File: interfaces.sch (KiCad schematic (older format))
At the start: 63 parts, among them J4 WE_629105150521, J6 685119134923, J7 1140084168, U12 FT2232HQ

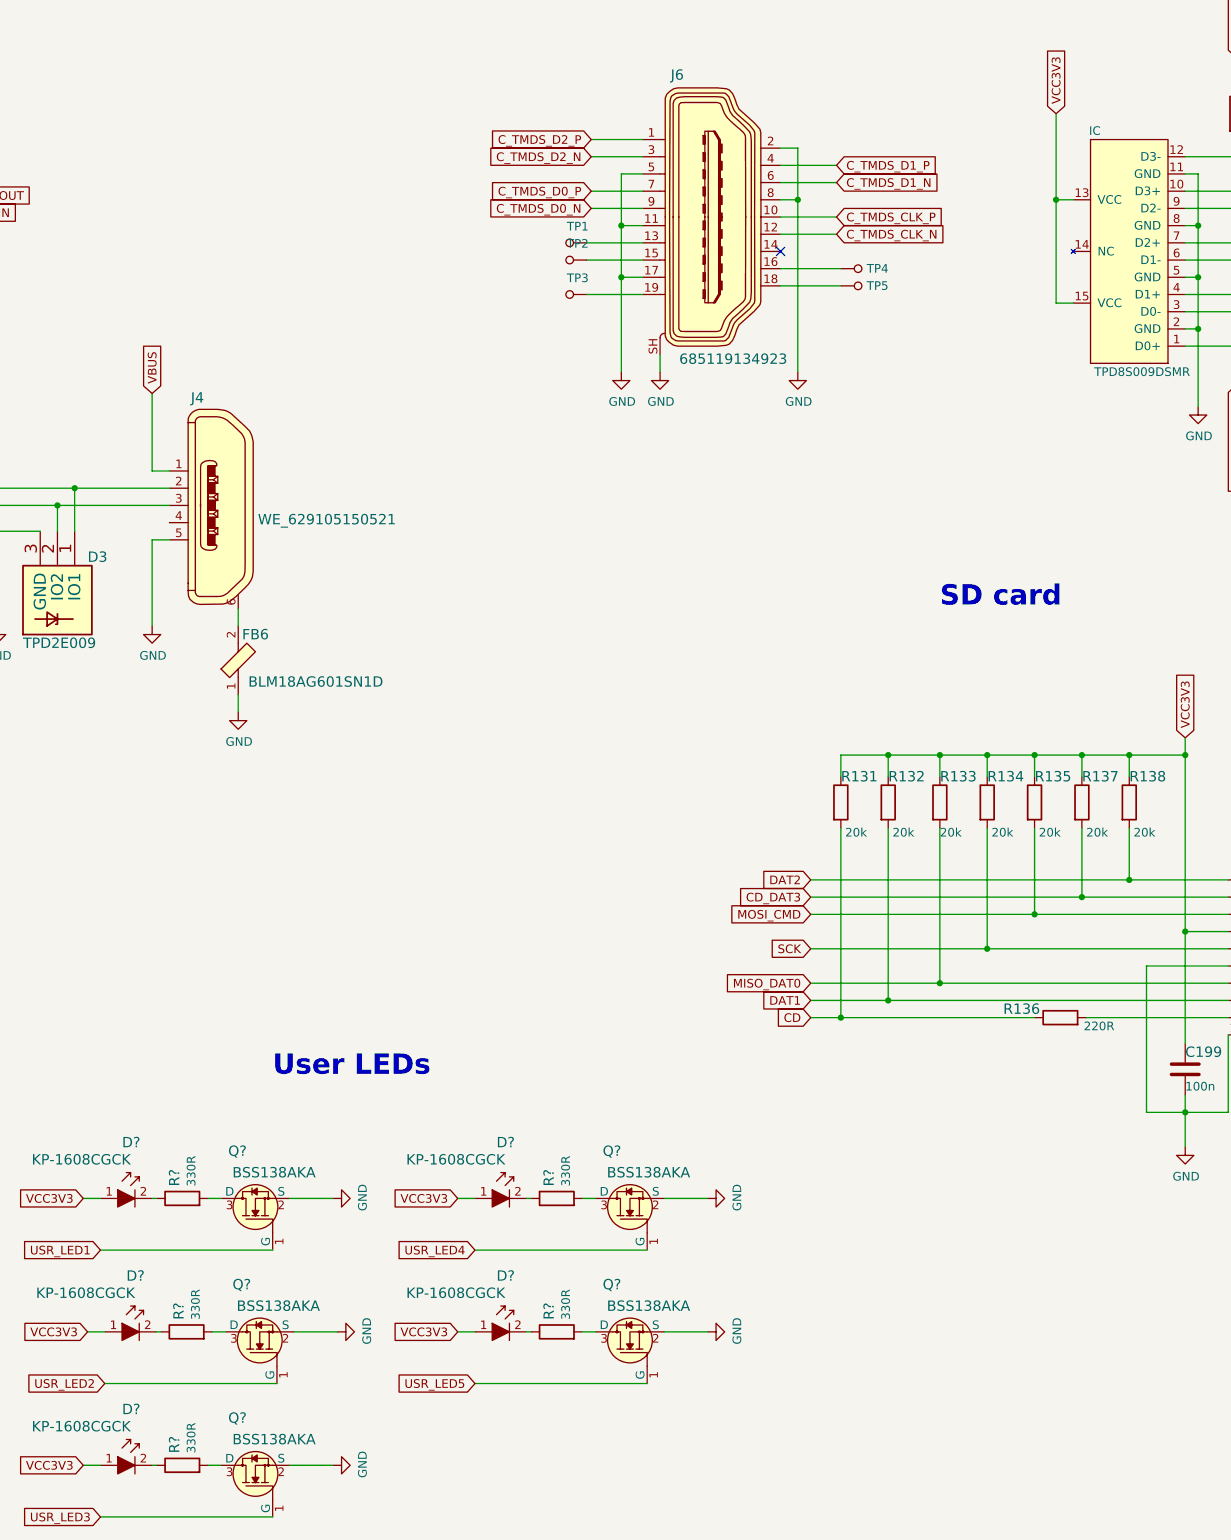
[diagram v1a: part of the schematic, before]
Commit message: Library cleanup, add RGMII layout
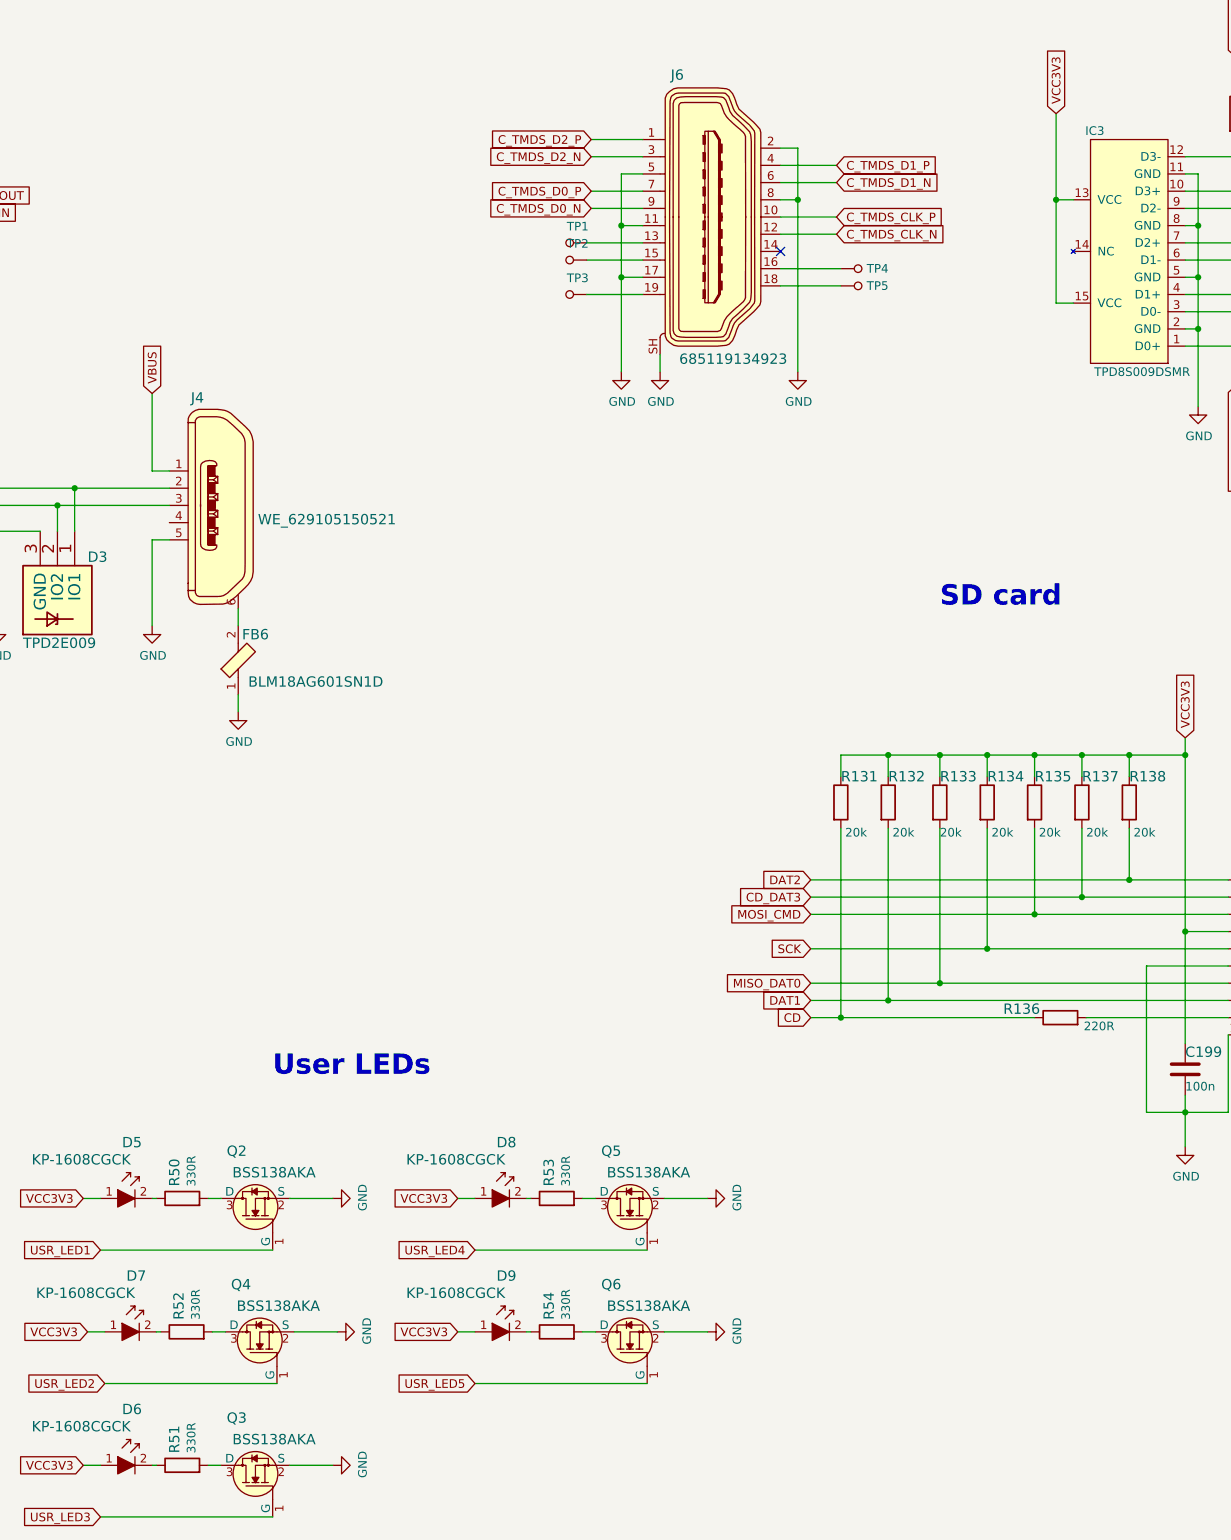
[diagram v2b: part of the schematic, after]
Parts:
- gave numbers to parts that had none: 15
- renumbered IC to IC3
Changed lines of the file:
@@
 $EndComp
 $Comp
-L lpddr4-test-board:TPD8S009DSMR IC
+L lpddr4-test-board:TPD8S009DSMR IC3
 U 1 1 601C2CA9
 P 13000 3625
-F 0 "IC" H 13225 2625 50  0000 C CNN
+F 0 "IC3" H 13225 2625 50  0000 C CNN
 F 1 "TPD8S009DSMR" H 12950 4025 50  0000 C CNN
 F 2 "lpddr4-test-board-footprints:R-PDSO-N15" H 14400 3275 50  0001 C CNN
@@
 	7800 5900 7800 6000
 $Comp
-L lpddr4-test-board:BSS138AKA Q?
+L lpddr4-test-board:BSS138AKA Q2
 U 1 1 5FF5BCFF
 P 7900 8825
-F 0 "Q?" V 8175 8875 60  0000 L CNN
+F 0 "Q2" V 8175 8875 60  0000 L CNN
 F 1 "BSS138AKA" V 8050 8475 60  0000 L CNN
 F 2 "lpddr4-test-board-footprints:SOT-23-3" H 8100 9025 60  0001 L CNN
@@
 $EndComp
 $Comp
-L lpddr4-test-board:GND #PWR?
+L lpddr4-test-board:GND #PWR0167
 U 1 1 5FF5DE33
 P 8350 8825
-F 0 "#PWR?" H 8350 8575 50  0001 C CNN
+F 0 "#PWR0167" H 8350 8575 50  0001 C CNN
 F 1 "GND" H 8355 8652 50  0000 C CNN
 F 2 "" H 8350 8825 50  0001 C CNN
@@
 	7700 8825 7625 8825
 $Comp
-L lpddr4-test-board:R_330R_0402 R?
+L lpddr4-test-board:R_330R_0402 R50
 U 1 1 5FF78200
 P 7475 8825
-F 0 "R?" V 7430 8895 60  0000 L CNN
+F 0 "R50" V 7430 8895 60  0000 L CNN
 F 1 "R_330R_0402" H 7475 8675 60  0001 C CNN
 F 2 "lpddr4-test-board-footprints:0402-res" H 7675 9025 60  0001 L CNN
@@
 $EndComp
 $Comp
-L lpddr4-test-board:KP-1608CGCK D?
+L lpddr4-test-board:KP-1608CGCK D5
 U 1 1 5FF856A4
 P 7200 8825
-F 0 "D?" H 7125 9150 60  0000 L CNN
+F 0 "D5" H 7125 9150 60  0000 L CNN
 F 1 "KP-1608CGCK" H 6600 9050 60  0000 L CNN
 F 2 "lpddr4-test-board-footprints:LED_0603" H 7400 9025 60  0001 L CNN
@@
 	8000 9125 7000 9125
 $Comp
-L lpddr4-test-board:BSS138AKA Q?
+L lpddr4-test-board:BSS138AKA Q4
 U 1 1 6002240B
 P 7925 9600
-F 0 "Q?" V 8200 9650 60  0000 L CNN
+F 0 "Q4" V 8200 9650 60  0000 L CNN
 F 1 "BSS138AKA" V 8075 9250 60  0000 L CNN
 F 2 "lpddr4-test-board-footprints:SOT-23-3" H 8125 9800 60  0001 L CNN
@@
 $EndComp
 $Comp
-L lpddr4-test-board:GND #PWR?
+L lpddr4-test-board:GND #PWR0168
 U 1 1 60022411
 P 8375 9600
-F 0 "#PWR?" H 8375 9350 50  0001 C CNN
+F 0 "#PWR0168" H 8375 9350 50  0001 C CNN
 F 1 "GND" H 8380 9427 50  0000 C CNN
 F 2 "" H 8375 9600 50  0001 C CNN
@@
 	7725 9600 7650 9600
 $Comp
-L lpddr4-test-board:R_330R_0402 R?
+L lpddr4-test-board:R_330R_0402 R52
 U 1 1 6002241C
 P 7500 9600
-F 0 "R?" V 7455 9670 60  0000 L CNN
+F 0 "R52" V 7455 9670 60  0000 L CNN
 F 1 "R_330R_0402" H 7500 9450 60  0001 C CNN
 F 2 "lpddr4-test-board-footprints:0402-res" H 7700 9800 60  0001 L CNN
@@
 $EndComp
 $Comp
-L lpddr4-test-board:KP-1608CGCK D?
+L lpddr4-test-board:KP-1608CGCK D7
 U 1 1 60022424
 P 7225 9600
-F 0 "D?" H 7150 9925 60  0000 L CNN
+F 0 "D7" H 7150 9925 60  0000 L CNN
 F 1 "KP-1608CGCK" H 6625 9825 60  0000 L CNN
 F 2 "lpddr4-test-board-footprints:LED_0603" H 7425 9800 60  0001 L CNN
@@
 	8025 9900 7025 9900
 $Comp
-L lpddr4-test-board:BSS138AKA Q?
+L lpddr4-test-board:BSS138AKA Q5
 U 1 1 600304B1
 P 10075 8825
-F 0 "Q?" V 10350 8875 60  0000 L CNN
+F 0 "Q5" V 10350 8875 60  0000 L CNN
 F 1 "BSS138AKA" V 10225 8475 60  0000 L CNN
 F 2 "lpddr4-test-board-footprints:SOT-23-3" H 10275 9025 60  0001 L CNN
@@
 $EndComp
 $Comp
-L lpddr4-test-board:GND #PWR?
+L lpddr4-test-board:GND #PWR0169
 U 1 1 600304B7
 P 10525 8825
-F 0 "#PWR?" H 10525 8575 50  0001 C CNN
+F 0 "#PWR0169" H 10525 8575 50  0001 C CNN
 F 1 "GND" H 10530 8652 50  0000 C CNN
 F 2 "" H 10525 8825 50  0001 C CNN
@@
 	9875 8825 9800 8825
 $Comp
-L lpddr4-test-board:R_330R_0402 R?
+L lpddr4-test-board:R_330R_0402 R53
 U 1 1 600304C2
 P 9650 8825
-F 0 "R?" V 9605 8895 60  0000 L CNN
+F 0 "R53" V 9605 8895 60  0000 L CNN
 F 1 "R_330R_0402" H 9650 8675 60  0001 C CNN
 F 2 "lpddr4-test-board-footprints:0402-res" H 9850 9025 60  0001 L CNN
@@
 $EndComp
 $Comp
-L lpddr4-test-board:KP-1608CGCK D?
+L lpddr4-test-board:KP-1608CGCK D8
 U 1 1 600304CA
 P 9375 8825
-F 0 "D?" H 9300 9150 60  0000 L CNN
+F 0 "D8" H 9300 9150 60  0000 L CNN
 F 1 "KP-1608CGCK" H 8775 9050 60  0000 L CNN
 F 2 "lpddr4-test-board-footprints:LED_0603" H 9575 9025 60  0001 L CNN
@@
 	10175 9125 9175 9125
 $Comp
-L lpddr4-test-board:BSS138AKA Q?
+L lpddr4-test-board:BSS138AKA Q6
 U 1 1 6003D8CD
 P 10075 9600
-F 0 "Q?" V 10350 9650 60  0000 L CNN
+F 0 "Q6" V 10350 9650 60  0000 L CNN
 F 1 "BSS138AKA" V 10225 9250 60  0000 L CNN
 F 2 "lpddr4-test-board-footprints:SOT-23-3" H 10275 9800 60  0001 L CNN
@@
 $EndComp
 $Comp
-L lpddr4-test-board:GND #PWR?
+L lpddr4-test-board:GND #PWR0170
 U 1 1 6003D8D3
 P 10525 9600
-F 0 "#PWR?" H 10525 9350 50  0001 C CNN
+F 0 "#PWR0170" H 10525 9350 50  0001 C CNN
 F 1 "GND" H 10530 9427 50  0000 C CNN
 F 2 "" H 10525 9600 50  0001 C CNN
@@
 	9875 9600 9800 9600
 $Comp
-L lpddr4-test-board:R_330R_0402 R?
+L lpddr4-test-board:R_330R_0402 R54
 U 1 1 6003D8DE
 P 9650 9600
-F 0 "R?" V 9605 9670 60  0000 L CNN
+F 0 "R54" V 9605 9670 60  0000 L CNN
 F 1 "R_330R_0402" H 9650 9450 60  0001 C CNN
 F 2 "lpddr4-test-board-footprints:0402-res" H 9850 9800 60  0001 L CNN
@@
 $EndComp
 $Comp
-L lpddr4-test-board:KP-1608CGCK D?
+L lpddr4-test-board:KP-1608CGCK D9
 U 1 1 6003D8E6
 P 9375 9600
-F 0 "D?" H 9300 9925 60  0000 L CNN
+F 0 "D9" H 9300 9925 60  0000 L CNN
 F 1 "KP-1608CGCK" H 8775 9825 60  0000 L CNN
 F 2 "lpddr4-test-board-footprints:LED_0603" H 9575 9800 60  0001 L CNN
@@
 	10175 9900 9175 9900
 $Comp
-L lpddr4-test-board:BSS138AKA Q?
+L lpddr4-test-board:BSS138AKA Q3
 U 1 1 60050B08
 P 7900 10375
-F 0 "Q?" V 8175 10425 60  0000 L CNN
+F 0 "Q3" V 8175 10425 60  0000 L CNN
 F 1 "BSS138AKA" V 8050 10025 60  0000 L CNN
 F 2 "lpddr4-test-board-footprints:SOT-23-3" H 8100 10575 60  0001 L CNN
@@
 $EndComp
 $Comp
-L lpddr4-test-board:GND #PWR?
+L lpddr4-test-board:GND #PWR0171
 U 1 1 60050B0E
 P 8350 10375
-F 0 "#PWR?" H 8350 10125 50  0001 C CNN
+F 0 "#PWR0171" H 8350 10125 50  0001 C CNN
 F 1 "GND" H 8355 10202 50  0000 C CNN
 F 2 "" H 8350 10375 50  0001 C CNN
@@
 	7700 10375 7625 10375
 $Comp
-L lpddr4-test-board:R_330R_0402 R?
+L lpddr4-test-board:R_330R_0402 R51
 U 1 1 60050B19
 P 7475 10375
-F 0 "R?" V 7430 10445 60  0000 L CNN
+F 0 "R51" V 7430 10445 60  0000 L CNN
 F 1 "R_330R_0402" H 7475 10225 60  0001 C CNN
 F 2 "lpddr4-test-board-footprints:0402-res" H 7675 10575 60  0001 L CNN
@@
 $EndComp
 $Comp
-L lpddr4-test-board:KP-1608CGCK D?
+L lpddr4-test-board:KP-1608CGCK D6
 U 1 1 60050B21
 P 7200 10375
-F 0 "D?" H 7125 10700 60  0000 L CNN
+F 0 "D6" H 7125 10700 60  0000 L CNN
 F 1 "KP-1608CGCK" H 6600 10600 60  0000 L CNN
 F 2 "lpddr4-test-board-footprints:LED_0603" H 7400 10575 60  0001 L CNN
